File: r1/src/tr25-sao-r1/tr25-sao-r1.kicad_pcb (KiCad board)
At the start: 2 copper layers, 46.8 x 68 mm, 1 part

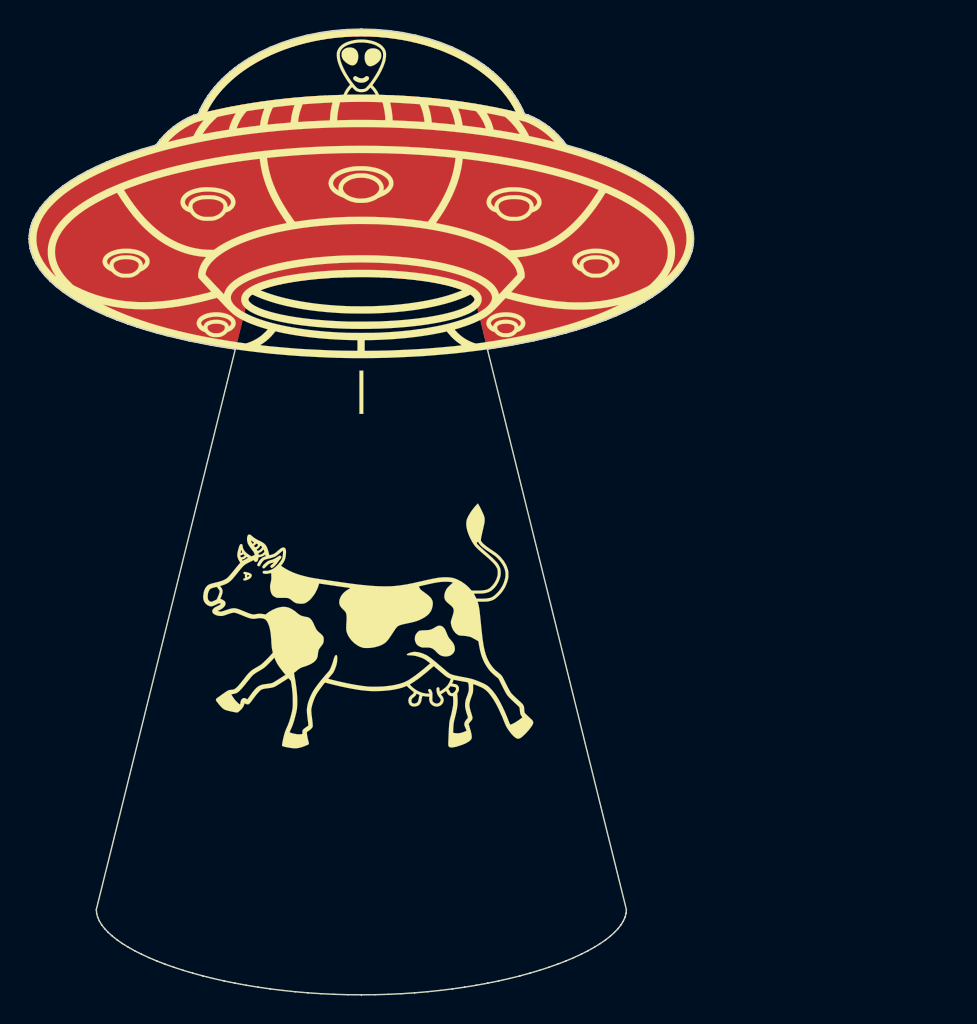
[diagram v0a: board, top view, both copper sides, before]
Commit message: jeffmakes Kicad library as submodule
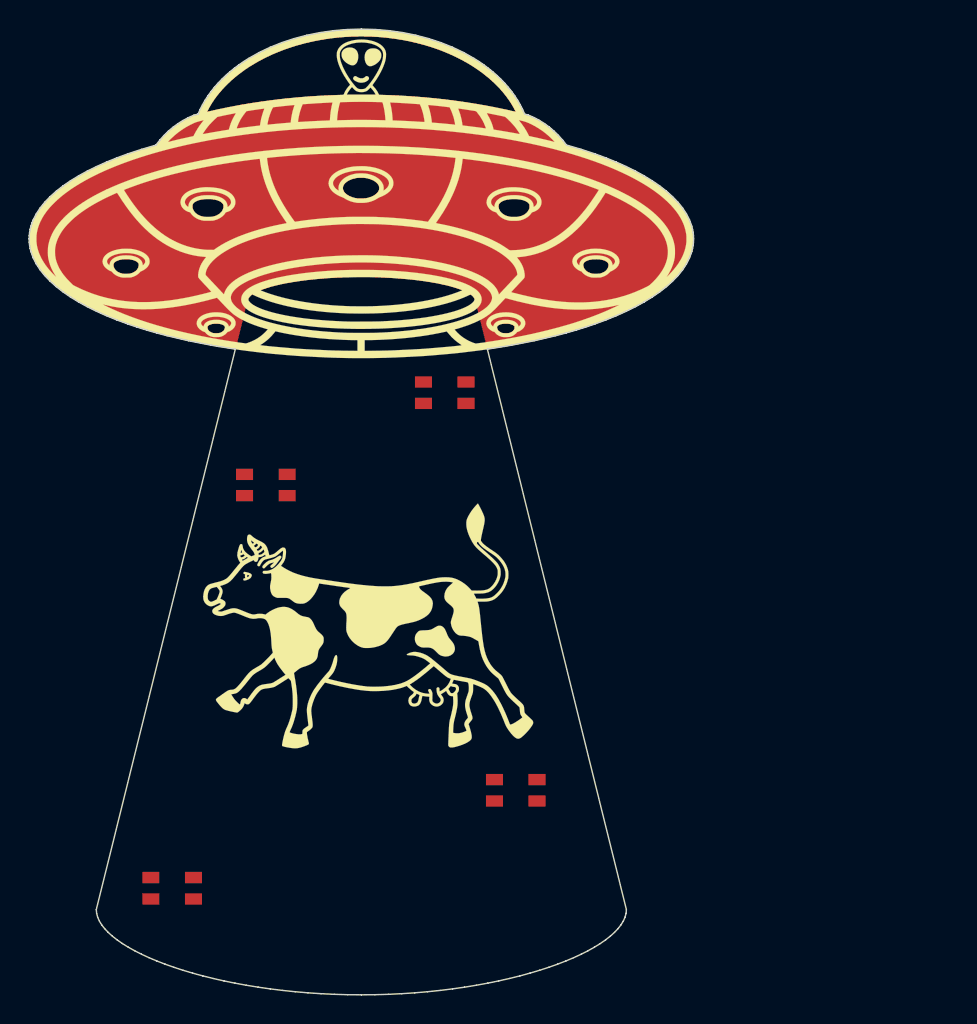
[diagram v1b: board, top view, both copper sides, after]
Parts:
- added D1: SK6812MINI, jeffmakes-footprints:LED_PLCC4_3.2x2.8mm_CCW, F.Cu at (55.3, 55.4)
- added D2: SK6812MINI, jeffmakes-footprints:LED_PLCC4_3.2x2.8mm_CCW, F.Cu at (42.7, 61.9)
- added D3: SK6812MINI, jeffmakes-footprints:LED_PLCC4_3.2x2.8mm_CCW, F.Cu at (60.3, 83.4)
- added D4: SK6812MINI, jeffmakes-footprints:LED_PLCC4_3.2x2.8mm_CCW, F.Cu at (36.1, 90.3)
- N1: value Housing -> Artwork

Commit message: Schematic complete, ERC pass
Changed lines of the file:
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@@
 		(embedded_fonts no)
+	)
+	(gr_circle
+		(center 40.7 60.2)
+		(end 40.9 60.2)
+		(stroke
+			(width 0.2)
+			(type default)
+		)
+		(fill no)
+		(layer "F.Cu")
+	)
+	(gr_circle
+		(center 58.3 81.7)
+		(end 58.5 81.7)
+		(stroke
+			(width 0.2)
+			(type default)
+		)
+		(fill no)
+		(layer "F.Cu")
+	)
+	(gr_circle
+		(center 34.1 88.6)
+		(end 34.3 88.6)
+		(stroke
+			(width 0.2)
+			(type default)
+		)
+		(fill no)
+		(layer "F.Cu")
+	)
+	(gr_circle
+		(center 53.3 53.7)
+		(end 53.5 53.7)
+		(stroke
+			(width 0.2)
+			(type default)
+		)
+		(fill no)
+		(layer "F.Cu")
 	)
 	(embedded_fonts no)

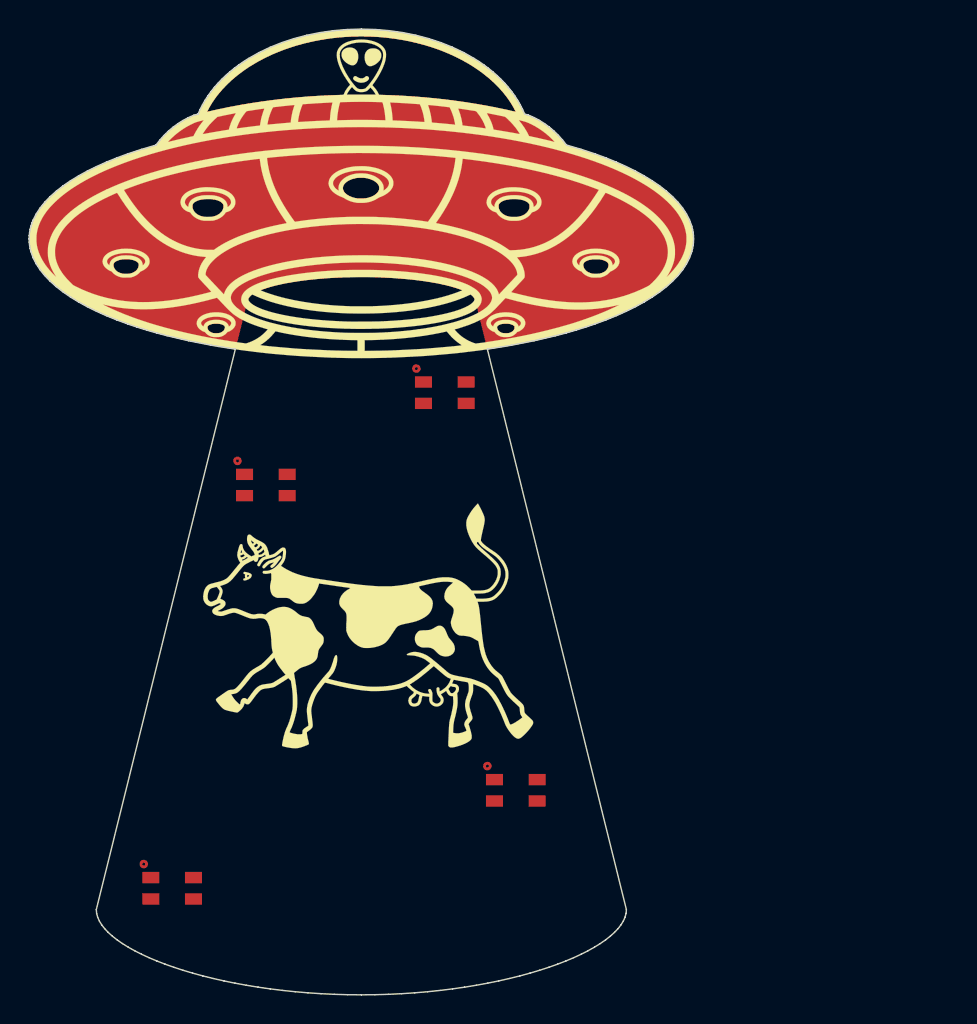
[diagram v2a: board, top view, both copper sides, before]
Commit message: Assign resistor footprints
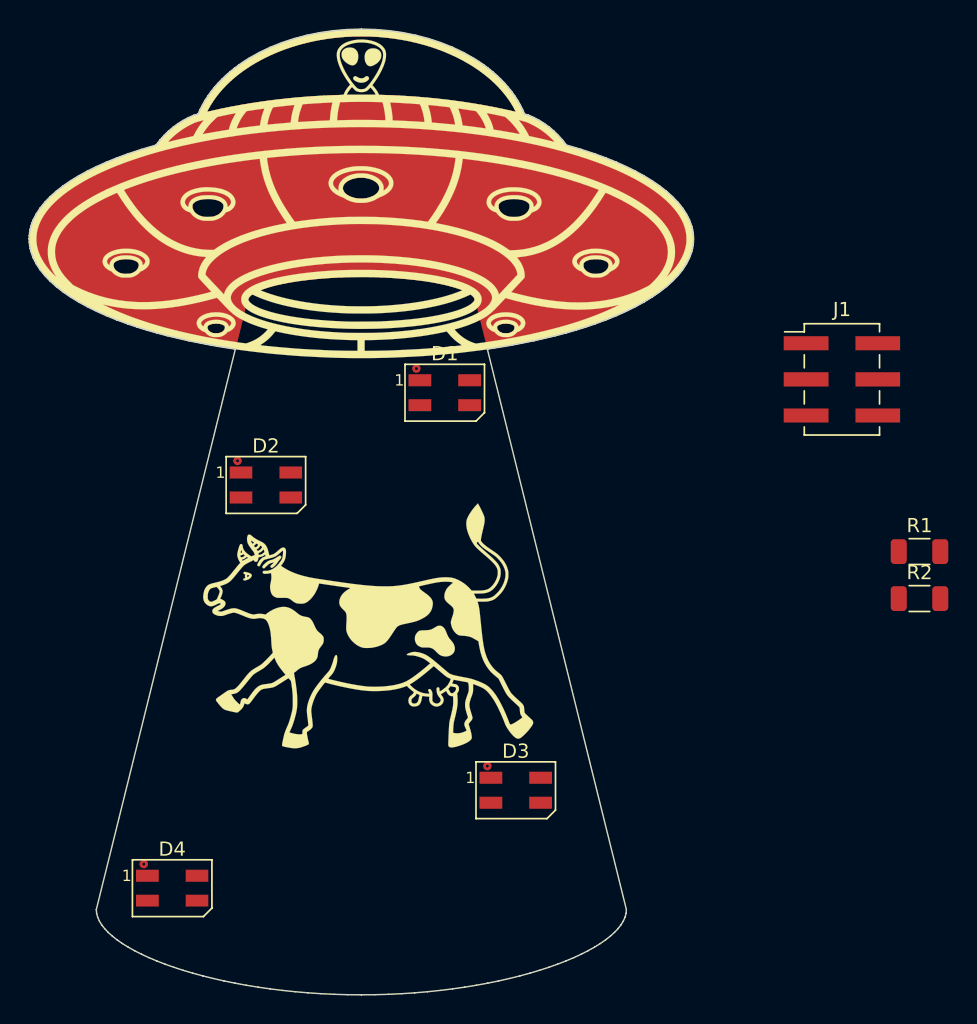
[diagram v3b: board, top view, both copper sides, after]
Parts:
- added J1: Conn_02x03_Odd_Even, Connector_PinHeader_2.54mm:PinHeader_2x03_P2.54mm_Vertical_SMD, F.Cu at (83.3, 54.5)
- added R1: 4k7, Resistor_SMD:R_1206_3216Metric, F.Cu at (88.7, 66.6)
- added R2: 220R, Resistor_SMD:R_1206_3216Metric, F.Cu at (88.7, 69.9)
- D1, D2, D3, D4: footprint jeffmakes-footprints:LED_PLCC4_3.2x2.8mm_CCW -> LED_SMD:LED_SK6812MINI_PLCC4_3.5x3.5mm_P1.75mm
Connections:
- D1 pad 1: unconnected-(D1-DOUT-Pad1) -> Net-(D1-DOUT)
- D1 pad 2: unconnected-(D1-VSS-Pad2) -> GND
- D1 pad 3: unconnected-(D1-DIN-Pad3) -> /IO2
- D1 pad 4: unconnected-(D1-VDD-Pad4) -> +3V3
- D2 pad 1: unconnected-(D2-DOUT-Pad1) -> Net-(D2-DOUT)
- D2 pad 2: unconnected-(D2-VSS-Pad2) -> GND
- D2 pad 3: unconnected-(D2-DIN-Pad3) -> Net-(D1-DOUT)
- D2 pad 4: unconnected-(D2-VDD-Pad4) -> +3V3
- D3 pad 1: unconnected-(D3-DOUT-Pad1) -> Net-(D3-DOUT)
- D3 pad 2: unconnected-(D3-VSS-Pad2) -> GND
- D3 pad 3: unconnected-(D3-DIN-Pad3) -> Net-(D2-DOUT)
- D3 pad 4: unconnected-(D3-VDD-Pad4) -> +3V3
- D4 pad 2: unconnected-(D4-VSS-Pad2) -> GND
- D4 pad 3: unconnected-(D4-DIN-Pad3) -> Net-(D3-DOUT)
- D4 pad 4: unconnected-(D4-VDD-Pad4) -> +3V3

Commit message: Correct LED pinout
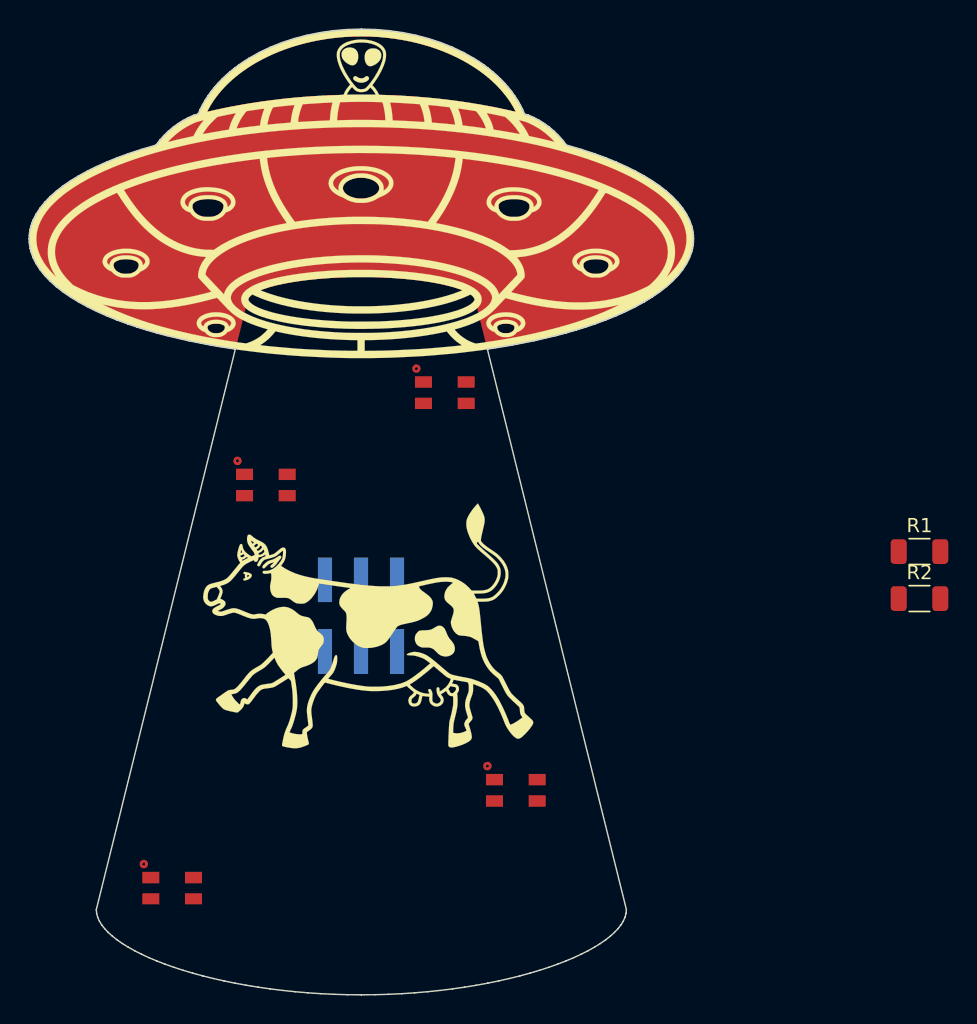
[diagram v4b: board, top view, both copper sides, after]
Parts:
- D1, D2, D3, D4: value SK6812MINI -> SK6812SMINI-ER; footprint LED_SMD:LED_SK6812MINI_PLCC4_3.5x3.5mm_P1.75mm -> jeffmakes-footprints:LED_PLCC4_3.2x2.8mm_CCW
- J1: moved to B.Cu
- moved J1 37.7 mm to (49.4, 71.1), turned to -90 degrees
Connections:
- D1 pad 1: Net-(D1-DOUT) -> GND
- D1 pad 2: GND -> /IO2
- D1 pad 3: /IO2 -> +3V3
- D1 pad 4: +3V3 -> /D1-DOUT
- D2 pad 1: Net-(D2-DOUT) -> GND
- D2 pad 2: GND -> /D1-DOUT
- D2 pad 3: Net-(D1-DOUT) -> +3V3
- D2 pad 4: +3V3 -> /D2-DOUT
- D3 pad 1: Net-(D3-DOUT) -> GND
- D3 pad 2: GND -> /D2-DOUT
- D3 pad 3: Net-(D2-DOUT) -> +3V3
- D3 pad 4: +3V3 -> /D3-DOUT
- D4 pad 1: unconnected-(D4-DOUT-Pad1) -> GND
- D4 pad 2: GND -> /D3-DOUT
- D4 pad 3: Net-(D3-DOUT) -> +3V3
- D4 pad 4: +3V3 -> unconnected-(D4-DOUT-Pad4)

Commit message: Routing complete. DRC pass
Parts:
- R1: value 4k7 -> 4.7k; moved to B.Cu
- R2: moved to B.Cu
- moved R1 36.6 mm to (52.8, 59.7), turned to 180 degrees
- moved R2 32.8 mm to (56.3, 65.3), turned to -90 degrees
- moved D1 1.11 mm to (54.4, 56.0)
- moved D4 0.86 mm to (36.3, 91.1)
- moved D3 0.76 mm to (60.6, 84.1)
- moved D2 0.58 mm to (43.3, 62.0)
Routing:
- net GND: track 0.00 -> 108.1 mm, vias 0 -> 4
- net +3V3: track 0.00 -> 87.4 mm, vias 0 -> 4
- net /D2-DOUT: track 0.00 -> 39.7 mm, vias 0 -> 2
- net /IO2: track 0.00 -> 39.5 mm, vias 0 -> 1
- net /D3-DOUT: track 0.00 -> 34.7 mm, vias 0 -> 2
- net /D1-DOUT: track 0.00 -> 21.2 mm, vias 0 -> 2
- net /IO1: track 0.00 -> 5.10 mm
